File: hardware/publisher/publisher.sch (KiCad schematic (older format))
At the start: 26 parts, among them J1 Main Connector, J2 Main Debug, J3 uC Debug, J4 Reset Switch, J5 HV Select, J6 CTRL Select, Q1 BC337, Q2 BC337, Q3 BC337, U1 WeMos_D1_mini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

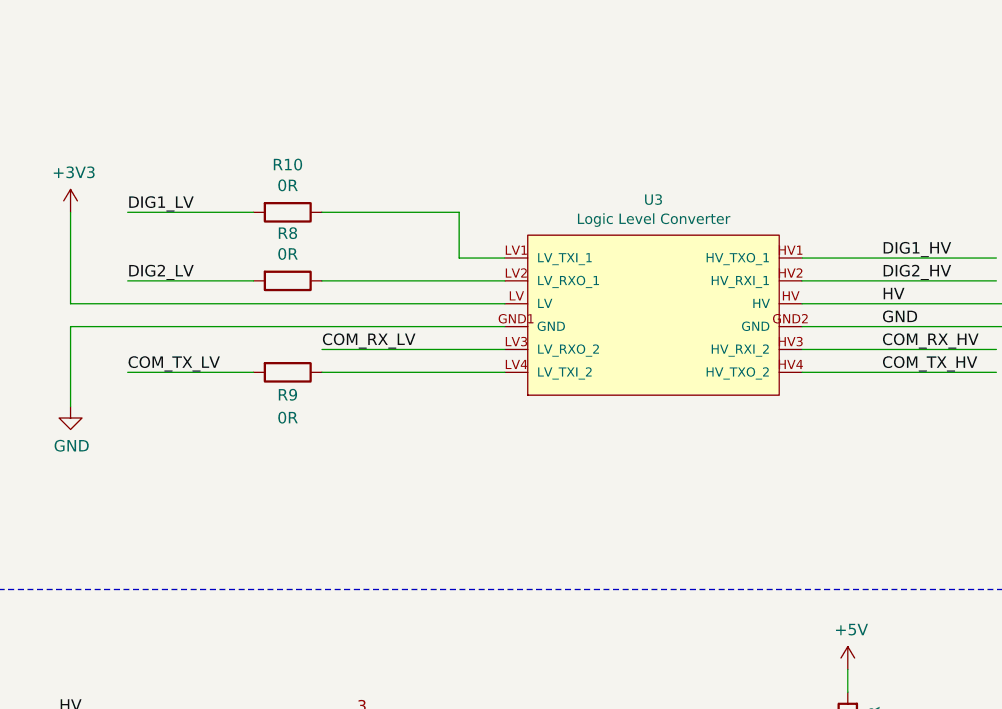
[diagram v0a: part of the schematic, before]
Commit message: schematic notes for 10k on R8 and removing R10
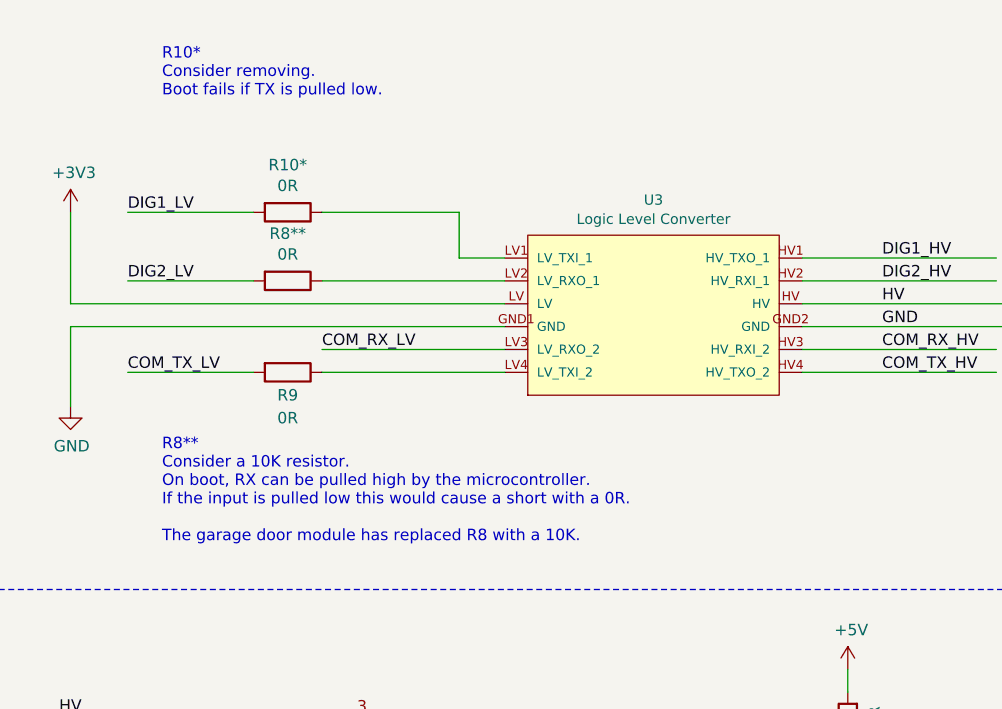
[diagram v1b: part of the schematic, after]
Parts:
- renumbered R10 to R10*, R8 to R8**
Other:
- note added: "R10*\nConsider removing.\nBoot fails if TX is pulled low.\n"
- note added: "R8**\nConsider a 10K resistor. \nOn boot, RX can be pulled high by the microcontroller. \nIf the input is pulled low this would cause a short with a 0R.\n\nThe garage door module has replaced R8 with a 10K."
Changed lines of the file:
@@
 $EndComp
 $Comp
-L Device:R R8
+L Device:R R8**
 U 1 1 60D9FD34
 P 6350 1650
-F 0 "R8" V 6143 1650 50  0000 C CNN
+F 0 "R8**" V 6143 1650 50  0000 C CNN
 F 1 "0R" V 6234 1650 50  0000 C CNN
 F 2 "Resistor_THT:R_Axial_DIN0207_L6.3mm_D2.5mm_P10.16mm_Horizontal" V 6280 1650 50  0001 C CNN
@@
 	9650 1850 9650 2200
 $Comp
-L Device:R R10
+L Device:R R10*
 U 1 1 60EF6109
 P 6350 1350
-F 0 "R10" V 6143 1350 50  0000 C CNN
+F 0 "R10*" V 6143 1350 50  0000 C CNN
 F 1 "0R" V 6234 1350 50  0000 C CNN
 F 2 "Resistor_THT:R_Axial_DIN0207_L6.3mm_D2.5mm_P10.16mm_Horizontal" V 6280 1350 50  0001 C CNN
@@
 Text Notes 2950 5600 0    50   ~ 0
 6-July-2021 - Added 500ohms in series on the \nCOM_RX_HV input (2x 1k in parallel).  Intent to \nstop the random panel tamper alarm.\n\nBattery = 13.86V\nLAN Power = 13.88V\nComms = 15V\n15v / 500ohms = 30mA
+Text Notes 5800 2800 0    50   ~ 0
+R8**\nConsider a 10K resistor.  \nOn boot, RX can be pulled high by the microcontroller. \nIf the input is pulled low this would cause a short with a 0R.\n\nThe garage door module has replaced R8 with a 10K.
+Text Notes 5800 850  0    50   ~ 0
+R10*\nConsider removing.\nBoot fails if TX is pulled low.\n
 $EndSCHEMATC
